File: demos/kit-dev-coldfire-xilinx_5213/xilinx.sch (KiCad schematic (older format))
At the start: 21 parts, among them P1 CONN_6, P3 CONN_2X2, P4 CONN_20X2, U9 XCR3256-TQ144

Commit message: Update demos to use sym-lib-table and recent libraries
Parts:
- C51, C52, C53, C54, C55, C56, C57, C58, C59, C60, C61: symbol C -> kit-dev-coldfire-xilinx_5213_schlib:C
- D8, D9: symbol LED -> kit-dev-coldfire-xilinx_5213_schlib:LED
- P1: symbol CONN_6 -> kit-dev-coldfire-xilinx_5213_schlib:CONN_6
- P3: symbol CONN_2X2 -> kit-dev-coldfire-xilinx_5213_schlib:CONN_2X2
- P4: symbol CONN_20X2 -> kit-dev-coldfire-xilinx_5213_schlib:CONN_20X2
- R57, R62, R63, R64: symbol R -> kit-dev-coldfire-xilinx_5213_schlib:R
- U9: symbol XCR3256-TQ144 -> kit-dev-coldfire-xilinx_5213_schlib:XCR3256-TQ144
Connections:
- wire segments 172 -> 149
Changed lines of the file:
@@
-EESchema Schematic File Version 2
-LIBS:power
-LIBS:device
-LIBS:transistors
-LIBS:conn
-LIBS:linear
-LIBS:regul
-LIBS:74xx
-LIBS:adc-dac
-LIBS:memory
-LIBS:xilinx
-LIBS:special
-LIBS:microcontrollers
-LIBS:motorola
+EESchema Schematic File Version 4
 LIBS:kit-dev-coldfire-xilinx_5213-cache
-EELAYER 25 0
+EELAYER 26 0
 EELAYER END
 $Descr A4 11693 8268
@@
 	3600 3800 3400 3800
 Wire Wire Line
-	10600 6350 10600 6400
+	10600 6400 10600 6350
 Connection ~ 10000 6400
 Wire Wire Line
@@
 	8800 6400 8800 6350
 Wire Wire Line
-	10600 6400 10300 6400
-Wire Wire Line
-	10300 6400 10000 6400
-Wire Wire Line
-	10000 6400 9700 6400
-Wire Wire Line
-	9700 6400 9400 6400
-Wire Wire Line
-	9400 6400 9100 6400
-Wire Wire Line
-	9100 6400 8800 6400
-Wire Wire Line
-	8800 6400 8500 6400
-Wire Wire Line
-	8500 6400 8200 6400
-Wire Wire Line
-	8200 6400 7900 6400
-Wire Wire Line
-	7900 6400 7600 6400
-Wire Wire Line
-	7600 5900 7900 5900
-Wire Wire Line
-	7900 5900 8200 5900
-Wire Wire Line
-	8200 5900 8500 5900
-Wire Wire Line
-	8500 5900 8800 5900
-Wire Wire Line
-	8800 5900 9100 5900
-Wire Wire Line
-	9100 5900 9400 5900
-Wire Wire Line
-	9400 5900 9700 5900
-Wire Wire Line
-	9700 5900 10000 5900
-Wire Wire Line
-	10000 5900 10300 5900
-Wire Wire Line
-	10300 5900 10600 5900
+	7600 6400 10600 6400
+Wire Wire Line
+	7600 5900 10600 5900
 Connection ~ 9700 5900
 Connection ~ 9100 5900
@@
 Connection ~ 7600 5900
 Wire Wire Line
-	7600 5950 7600 5900
-Wire Wire Line
-	7600 5900 7600 5850
+	7600 5850 7600 5950
 Connection ~ 10000 5900
 Connection ~ 7900 5900
@@
 	10000 5900 10000 5950
 Wire Wire Line
-	7600 6450 7600 6400
-Wire Wire Line
-	7600 6400 7600 6350
+	7600 6350 7600 6450
 Connection ~ 7600 6400
 Wire Wire Line
@@
 	3450 1200 3450 1250
 Wire Wire Line
-	3600 900  3050 900
-Wire Wire Line
-	3050 900  2700 900
+	2700 900  3600 900
 Wire Wire Line
 	3600 3900 3550 3900
 Wire Wire Line
-	3550 3900 3550 4000
-Wire Wire Line
-	3550 4000 3550 4100
-Wire Wire Line
-	3500 4100 3550 4100
-Wire Wire Line
-	3550 4100 3600 4100
+	3550 3900 3550 4100
+Wire Wire Line
+	3500 4100 3600 4100
 Connection ~ 3550 4100
 Wire Wire Line
@@
 +3,3V_OUT
 $Comp
-L GND #PWR0105
+L kit-dev-coldfire-xilinx_5213_schlib:GND #PWR0105
 U 1 1 480DCF5A
 P 3500 4100
@@
 $EndComp
 $Comp
-L +3,3V #PWR0106
+L kit-dev-coldfire-xilinx_5213_schlib:+3,3V #PWR0106
 U 1 1 4791D619
 P 10850 3900
@@
 $EndComp
 $Comp
-L R R64
+L kit-dev-coldfire-xilinx_5213_schlib:R R64
 U 1 1 4791D59D
 P 10450 3900
@@
 NoConn ~ 5500 900
 $Comp
-L GND #PWR0107
+L kit-dev-coldfire-xilinx_5213_schlib:GND #PWR0107
 U 1 1 470F3BF2
 P 3450 1250
@@
 XIL_IRQ1
 $Comp
-L CONN_2X2 P3
+L kit-dev-coldfire-xilinx_5213_schlib:CONN_2X2 P3
 U 1 1 46A76EB2
 P 6600 1250
@@
 $EndComp
 $Comp
-L XCR3256-TQ144 U9
+L kit-dev-coldfire-xilinx_5213_schlib:XCR3256-TQ144 U9
 U 1 1 470F38BE
 P 4550 4100
@@
 XIL_D35
 $Comp
-L GND #PWR0108
+L kit-dev-coldfire-xilinx_5213_schlib:GND #PWR0108
 U 1 1 46ADE620
 P 9650 4000
@@
 $EndComp
 $Comp
-L GND #PWR0109
+L kit-dev-coldfire-xilinx_5213_schlib:GND #PWR0109
 U 1 1 46ADE61B
 P 9650 2100
@@
 XIL_D6
 $Comp
-L CONN_20X2 P4
+L kit-dev-coldfire-xilinx_5213_schlib:CONN_20X2 P4
 U 1 1 46ADE55A
 P 9200 3050
@@
 GLCK2
 $Comp
-L +3,3V #PWR0110
+L kit-dev-coldfire-xilinx_5213_schlib:+3,3V #PWR0110
 U 1 1 46A76BD3
 P 2750 1300
@@
 $EndComp
 $Comp
-L +3,3V #PWR0111
+L kit-dev-coldfire-xilinx_5213_schlib:+3,3V #PWR0111
 U 1 1 46A76BD2
 P 3600 650
@@
 $EndComp
 $Comp
-L R R57
+L kit-dev-coldfire-xilinx_5213_schlib:R R57
 U 1 1 46A76BCA
 P 3300 650
@@
 LED_TEST1
 $Comp
-L GND #PWR0112
+L kit-dev-coldfire-xilinx_5213_schlib:GND #PWR0112
 U 1 1 46A76BC5
 P 10050 5100
@@
 $EndComp
 $Comp
-L LED D8
+L kit-dev-coldfire-xilinx_5213_schlib:LED D8
 U 1 1 46A76BC4
 P 9800 5100
@@
 $EndComp
 $Comp
-L R R62
+L kit-dev-coldfire-xilinx_5213_schlib:R R62
 U 1 1 46A76BC3
 P 9250 5100
@@
 $EndComp
 $Comp
-L GND #PWR0113
+L kit-dev-coldfire-xilinx_5213_schlib:GND #PWR0113
 U 1 1 46A76BC1
 P 7600 6450
@@
 $EndComp
 $Comp
-L +3,3V #PWR0114
+L kit-dev-coldfire-xilinx_5213_schlib:+3,3V #PWR0114
 U 1 1 46A76BBF
 P 7600 5850
@@
 $EndComp
 $Comp
-L C C61
+L kit-dev-coldfire-xilinx_5213_schlib:C C61
 U 1 1 46A76BBC
 P 10600 6150
@@
 $EndComp
 $Comp
-L C C60
+L kit-dev-coldfire-xilinx_5213_schlib:C C60
 U 1 1 46A76BBB
 P 10300 6150
@@
 $EndComp
 $Comp
-L C C59
+L kit-dev-coldfire-xilinx_5213_schlib:C C59
 U 1 1 46A76BBA
 P 10000 6150
@@
 $EndComp
 $Comp
-L C C54
+L kit-dev-coldfire-xilinx_5213_schlib:C C54
 U 1 1 46A76BB5
 P 8500 6150
@@
 $EndComp
 $Comp
-L C C53
+L kit-dev-coldfire-xilinx_5213_schlib:C C53
 U 1 1 46A76BB4
 P 8200 6150
@@
 $EndComp
 $Comp
-L C C52
+L kit-dev-coldfire-xilinx_5213_schlib:C C52
 U 1 1 46A76BB3
 P 7900 6150
@@
 $EndComp
 $Comp
-L C C51
+L kit-dev-coldfire-xilinx_5213_schlib:C C51
 U 1 1 46A76BB2
 P 7600 6150
@@
 $EndComp
 $Comp
-L C C58
+L kit-dev-coldfire-xilinx_5213_schlib:C C58
 U 1 1 46A76BB1
 P 9700 6150
@@
 $EndComp
 $Comp
-L C C57
+L kit-dev-coldfire-xilinx_5213_schlib:C C57
 U 1 1 46A76BB0
 P 9400 6150
@@
 $EndComp
 $Comp
-L C C56
+L kit-dev-coldfire-xilinx_5213_schlib:C C56
 U 1 1 46A76BAF
 P 9100 6150
@@
 $EndComp
 $Comp
-L C C55
+L kit-dev-coldfire-xilinx_5213_schlib:C C55
 U 1 1 46A76BAE
 P 8800 6150
@@
 TCK
 $Comp
-L GND #PWR0115
+L kit-dev-coldfire-xilinx_5213_schlib:GND #PWR0115
 U 1 1 46A76BA9
 P 10050 5400
@@
 $EndComp
 $Comp
-L LED D9
+L kit-dev-coldfire-xilinx_5213_schlib:LED D9
 U 1 1 46A76BA8
 P 9800 5400
@@
 $EndComp
 $Comp
-L R R63
+L kit-dev-coldfire-xilinx_5213_schlib:R R63
 U 1 1 46A76BA7
 P 9250 5400
@@
 TDO
 $Comp
-L CONN_6 P1
+L kit-dev-coldfire-xilinx_5213_schlib:CONN_6 P1
 U 1 1 46A76BA6
 P 2350 1050
@@
 $EndComp
 $Comp
-L GND #PWR0116
+L kit-dev-coldfire-xilinx_5213_schlib:GND #PWR0116
 U 1 1 46A76BA5
 P 2750 1200

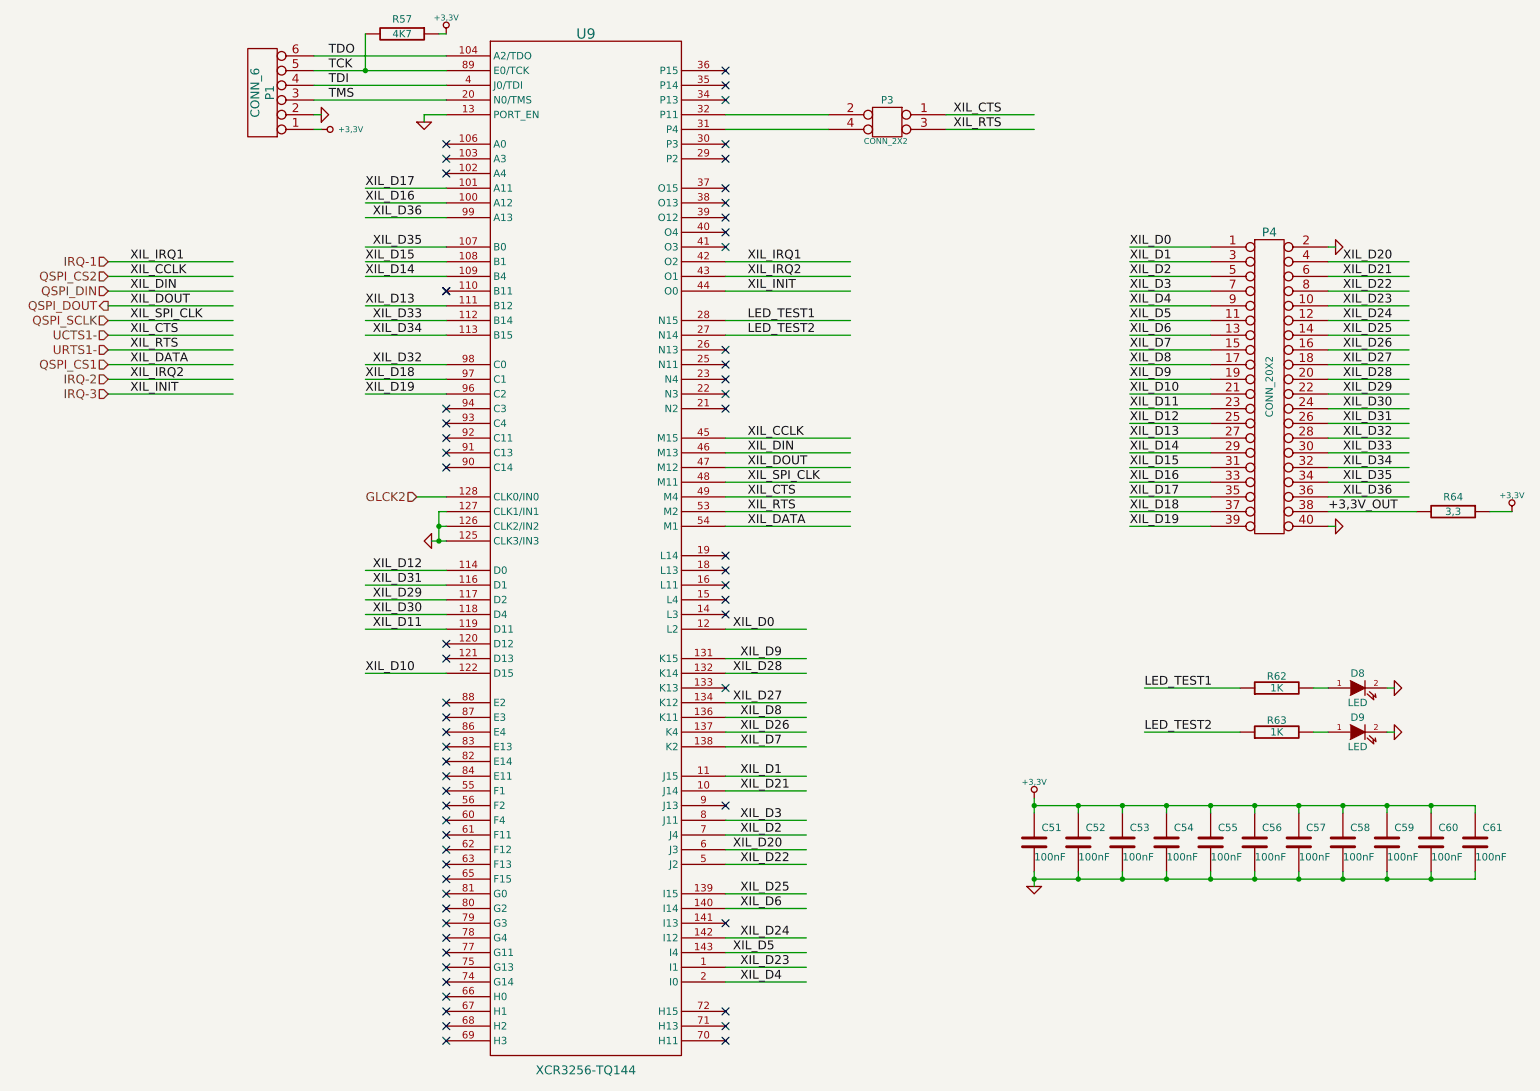
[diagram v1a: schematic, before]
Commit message: Update demo to use V5 libraries.
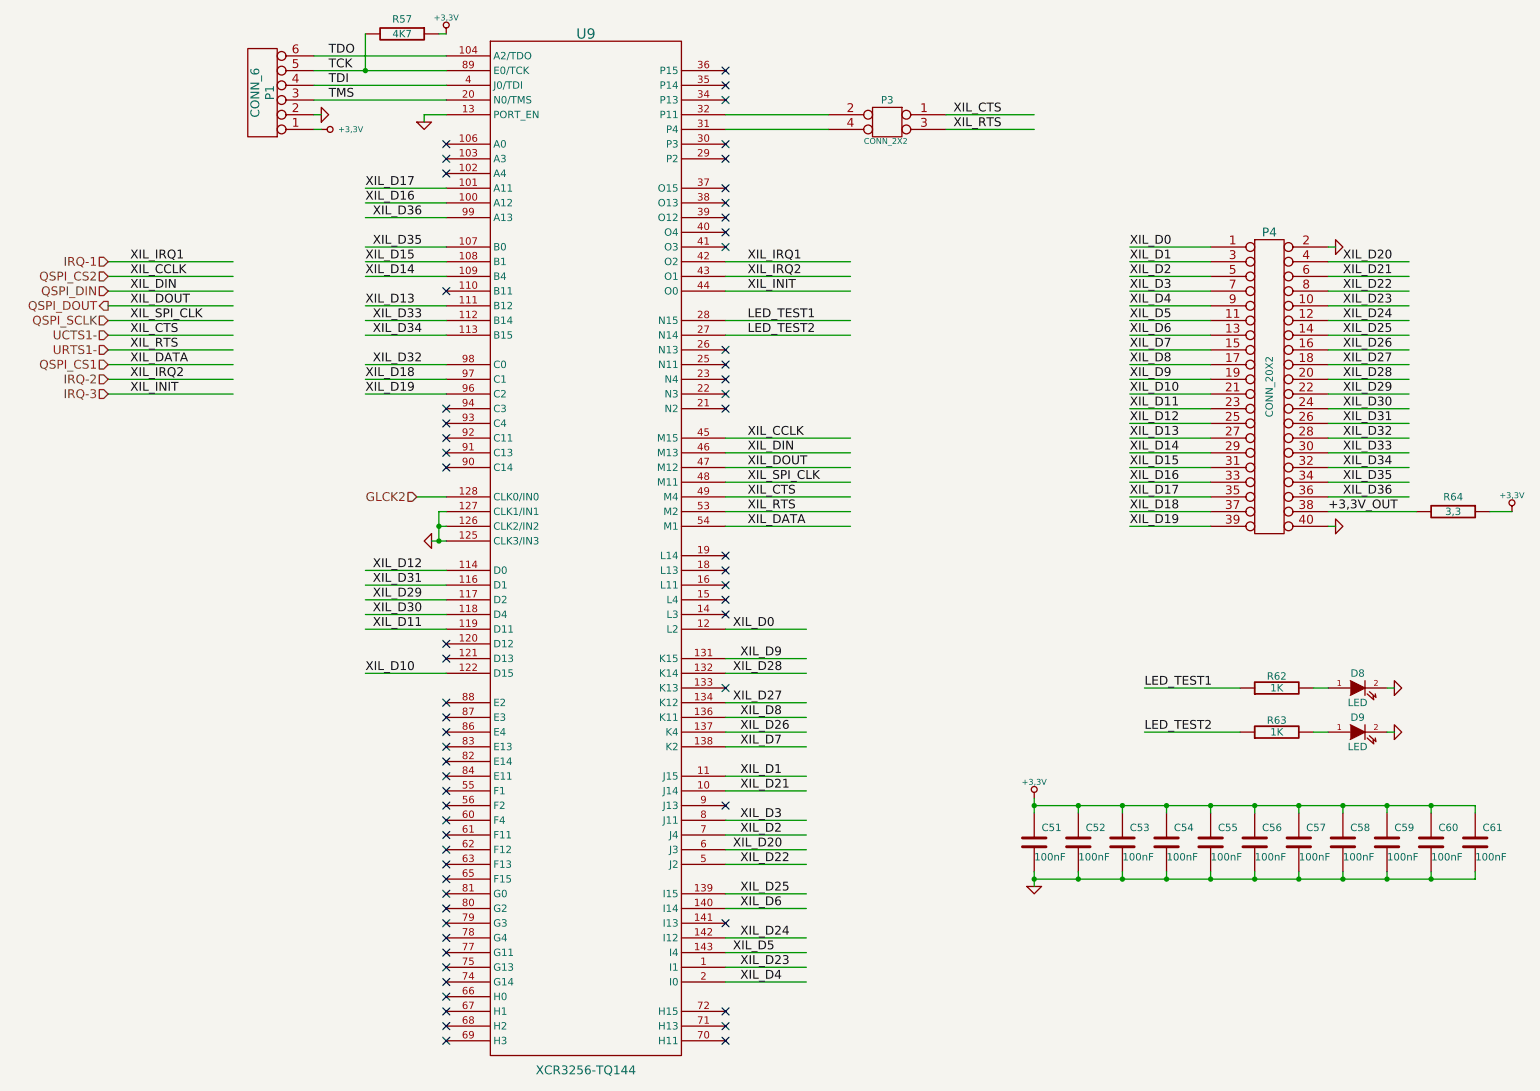
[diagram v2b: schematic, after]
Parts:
- C51, C52, C53, C54, C55, C56, C57, C58, C59, C60, C61, R57, R62, R63: footprint lib_smd:SM0805 -> Resistor_SMD:R_0805_2012Metric
- D8, D9: footprint lib_smd:SM1206POL -> LED_SMD:LED_1206_3216Metric
- P1: footprint pin_array:PIN_ARRAY-6X1 -> Connector_PinHeader_2.54mm:PinHeader_1x06_P2.54mm_Vertical
- P3: footprint pin_array:PIN_ARRAY_2X2 -> Connector_PinHeader_2.54mm:PinHeader_2x02_P2.54mm_Vertical
- P4: footprint pin_array:PIN_ARRAY_20X2 -> Connector_PinHeader_2.54mm:PinHeader_2x20_P2.54mm_Vertical
- R64: footprint discret:R4 -> Resistor_THT:R_Axial_DIN0207_L6.3mm_D2.5mm_P10.16mm_Horizontal
- U9: footprint lib_smd:TQFP144 -> Package_QFP:TQFP-144_20x20mm_P0.5mm
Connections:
- wire segments 149 -> 172
- no-connect marks 62 -> 61
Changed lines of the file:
@@
 NoConn ~ 3600 3300
 NoConn ~ 3600 3200
-NoConn ~ 3600 2400
 NoConn ~ 3600 4900
 NoConn ~ 3600 4800
@@
 	8800 6400 8800 6350
 Wire Wire Line
-	7600 6400 10600 6400
-Wire Wire Line
-	7600 5900 10600 5900
+	7600 6400 7900 6400
+Wire Wire Line
+	7600 5900 7900 5900
 Connection ~ 9700 5900
 Connection ~ 9100 5900
@@
 Connection ~ 7600 5900
 Wire Wire Line
-	7600 5850 7600 5950
+	7600 5850 7600 5900
 Connection ~ 10000 5900
 Connection ~ 7900 5900
@@
 	10000 5900 10000 5950
 Wire Wire Line
-	7600 6350 7600 6450
+	7600 6350 7600 6400
 Connection ~ 7600 6400
 Wire Wire Line
@@
 	3450 1200 3450 1250
 Wire Wire Line
-	2700 900  3600 900
+	2700 900  3050 900
 Wire Wire Line
 	3600 3900 3550 3900
 Wire Wire Line
-	3550 3900 3550 4100
-Wire Wire Line
-	3500 4100 3600 4100
+	3550 3900 3550 4000
+Wire Wire Line
+	3500 4100 3550 4100
 Connection ~ 3550 4100
 Wire Wire Line
@@
 F 0 "R64" V 10350 3900 50  0000 C CNN
 F 1 "3,3" V 10450 3900 50  0000 C CNN
-F 2 "discret:R4" H 10450 3900 60  0001 C CNN
+F 2 "Resistor_THT:R_Axial_DIN0207_L6.3mm_D2.5mm_P10.16mm_Horizontal" H 10450 3900 60  0001 C CNN
 F 3 "" H 10450 3900 60  0001 C CNN
 	1    10450 3900
@@
 F 0 "P3" H 6600 1400 50  0000 C CNN
 F 1 "CONN_2X2" H 6610 1120 40  0000 C CNN
-F 2 "pin_array:PIN_ARRAY_2X2" H 6600 1250 60  0001 C CNN
+F 2 "Connector_PinHeader_2.54mm:PinHeader_2x02_P2.54mm_Vertical" H 6600 1250 60  0001 C CNN
 F 3 "" H 6600 1250 60  0001 C CNN
 	1    6600 1250
@@
 F 0 "U9" H 4550 7550 70  0000 C CNN
 F 1 "XCR3256-TQ144" H 4550 500 60  0000 C CNN
-F 2 "lib_smd:TQFP144" H 4550 4100 60  0001 C CNN
+F 2 "Package_QFP:TQFP-144_20x20mm_P0.5mm" H 4550 4100 60  0001 C CNN
 F 3 "" H 4550 4100 60  0001 C CNN
 	1    4550 4100
@@
 F 0 "P4" H 9200 4100 60  0000 C CNN
 F 1 "CONN_20X2" V 9200 3050 50  0000 C CNN
-F 2 "pin_array:PIN_ARRAY_20X2" H 9200 3050 60  0001 C CNN
+F 2 "Connector_PinHeader_2.54mm:PinHeader_2x20_P2.54mm_Vertical" H 9200 3050 60  0001 C CNN
 F 3 "" H 9200 3050 60  0001 C CNN
 	1    9200 3050
@@
 F 0 "R57" V 3200 650 50  0000 C CNN
 F 1 "4K7" V 3300 650 50  0000 C CNN
-F 2 "lib_smd:SM0805" H 3300 650 60  0001 C CNN
+F 2 "Resistor_SMD:R_0805_2012Metric" H 3300 650 60  0001 C CNN
 F 3 "" H 3300 650 60  0001 C CNN
 	1    3300 650
@@
 F 0 "D8" H 9800 5200 50  0000 C CNN
 F 1 "LED" H 9800 5000 50  0000 C CNN
-F 2 "lib_smd:SM1206POL" H 9800 5100 60  0001 C CNN
+F 2 "LED_SMD:LED_1206_3216Metric" H 9800 5100 60  0001 C CNN
 F 3 "" H 9800 5100 60  0001 C CNN
 	1    9800 5100
@@
 F 0 "R62" V 9330 5100 50  0000 C CNN
 F 1 "1K" V 9250 5100 50  0000 C CNN
-F 2 "lib_smd:SM0805" H 9250 5100 60  0001 C CNN
+F 2 "Resistor_SMD:R_0805_2012Metric" H 9250 5100 60  0001 C CNN
 F 3 "" H 9250 5100 60  0001 C CNN
 	1    9250 5100
@@
 F 0 "C61" H 10650 6250 50  0000 L CNN
 F 1 "100nF" H 10600 6050 50  0000 L CNN
-F 2 "lib_smd:SM0805" H 10600 6150 60  0001 C CNN
+F 2 "Resistor_SMD:R_0805_2012Metric" H 10600 6150 60  0001 C CNN
 F 3 "" H 10600 6150 60  0001 C CNN
 	1    10600 6150
@@
 F 0 "C60" H 10350 6250 50  0000 L CNN
 F 1 "100nF" H 10300 6050 50  0000 L CNN
-F 2 "lib_smd:SM0805" H 10300 6150 60  0001 C CNN
+F 2 "Resistor_SMD:R_0805_2012Metric" H 10300 6150 60  0001 C CNN
 F 3 "" H 10300 6150 60  0001 C CNN
 	1    10300 6150
@@
 F 0 "C59" H 10050 6250 50  0000 L CNN
 F 1 "100nF" H 10000 6050 50  0000 L CNN
-F 2 "lib_smd:SM0805" H 10000 6150 60  0001 C CNN
+F 2 "Resistor_SMD:R_0805_2012Metric" H 10000 6150 60  0001 C CNN
 F 3 "" H 10000 6150 60  0001 C CNN
 	1    10000 6150
@@
 F 0 "C54" H 8550 6250 50  0000 L CNN
 F 1 "100nF" H 8500 6050 50  0000 L CNN
-F 2 "lib_smd:SM0805" H 8500 6150 60  0001 C CNN
+F 2 "Resistor_SMD:R_0805_2012Metric" H 8500 6150 60  0001 C CNN
 F 3 "" H 8500 6150 60  0001 C CNN
 	1    8500 6150
@@
 F 0 "C53" H 8250 6250 50  0000 L CNN
 F 1 "100nF" H 8200 6050 50  0000 L CNN
-F 2 "lib_smd:SM0805" H 8200 6150 60  0001 C CNN
+F 2 "Resistor_SMD:R_0805_2012Metric" H 8200 6150 60  0001 C CNN
 F 3 "" H 8200 6150 60  0001 C CNN
 	1    8200 6150
@@
 F 0 "C52" H 7950 6250 50  0000 L CNN
 F 1 "100nF" H 7900 6050 50  0000 L CNN
-F 2 "lib_smd:SM0805" H 7900 6150 60  0001 C CNN
+F 2 "Resistor_SMD:R_0805_2012Metric" H 7900 6150 60  0001 C CNN
 F 3 "" H 7900 6150 60  0001 C CNN
 	1    7900 6150
@@
 F 0 "C51" H 7650 6250 50  0000 L CNN
 F 1 "100nF" H 7600 6050 50  0000 L CNN
-F 2 "lib_smd:SM0805" H 7600 6150 60  0001 C CNN
+F 2 "Resistor_SMD:R_0805_2012Metric" H 7600 6150 60  0001 C CNN
 F 3 "" H 7600 6150 60  0001 C CNN
 	1    7600 6150
@@
 F 0 "C58" H 9750 6250 50  0000 L CNN
 F 1 "100nF" H 9700 6050 50  0000 L CNN
-F 2 "lib_smd:SM0805" H 9700 6150 60  0001 C CNN
+F 2 "Resistor_SMD:R_0805_2012Metric" H 9700 6150 60  0001 C CNN
 F 3 "" H 9700 6150 60  0001 C CNN
 	1    9700 6150
@@
 F 0 "C57" H 9450 6250 50  0000 L CNN
 F 1 "100nF" H 9400 6050 50  0000 L CNN
-F 2 "lib_smd:SM0805" H 9400 6150 60  0001 C CNN
+F 2 "Resistor_SMD:R_0805_2012Metric" H 9400 6150 60  0001 C CNN
 F 3 "" H 9400 6150 60  0001 C CNN
 	1    9400 6150
@@
 F 0 "C56" H 9150 6250 50  0000 L CNN
 F 1 "100nF" H 9100 6050 50  0000 L CNN
-F 2 "lib_smd:SM0805" H 9100 6150 60  0001 C CNN
+F 2 "Resistor_SMD:R_0805_2012Metric" H 9100 6150 60  0001 C CNN
 F 3 "" H 9100 6150 60  0001 C CNN
 	1    9100 6150
@@
 F 0 "C55" H 8850 6250 50  0000 L CNN
 F 1 "100nF" H 8800 6050 50  0000 L CNN
-F 2 "lib_smd:SM0805" H 8800 6150 60  0001 C CNN
+F 2 "Resistor_SMD:R_0805_2012Metric" H 8800 6150 60  0001 C CNN
 F 3 "" H 8800 6150 60  0001 C CNN
 	1    8800 6150
@@
 F 0 "D9" H 9800 5500 50  0000 C CNN
 F 1 "LED" H 9800 5300 50  0000 C CNN
-F 2 "lib_smd:SM1206POL" H 9800 5400 60  0001 C CNN
+F 2 "LED_SMD:LED_1206_3216Metric" H 9800 5400 60  0001 C CNN
 F 3 "" H 9800 5400 60  0001 C CNN
 	1    9800 5400
@@
 F 0 "R63" V 9330 5400 50  0000 C CNN
 F 1 "1K" V 9250 5400 50  0000 C CNN
-F 2 "lib_smd:SM0805" H 9250 5400 60  0001 C CNN
+F 2 "Resistor_SMD:R_0805_2012Metric" H 9250 5400 60  0001 C CNN
 F 3 "" H 9250 5400 60  0001 C CNN
 	1    9250 5400
@@
 F 0 "P1" V 2300 1050 60  0000 C CNN
 F 1 "CONN_6" V 2400 1050 60  0000 C CNN
-F 2 "pin_array:PIN_ARRAY-6X1" H 2350 1050 60  0001 C CNN
+F 2 "Connector_PinHeader_2.54mm:PinHeader_1x06_P2.54mm_Vertical" H 2350 1050 60  0001 C CNN
 F 3 "" H 2350 1050 60  0001 C CNN
 	1    2350 1050
@@
 Wire Wire Line
 	10000 5100 10050 5100
+Wire Wire Line
+	3050 900  3600 900
+Wire Wire Line
+	3550 4000 3550 4100
+Wire Wire Line
+	10000 6400 10300 6400
+Wire Wire Line
+	9400 6400 9700 6400
+Wire Wire Line
+	8800 6400 9100 6400
+Wire Wire Line
+	9700 5900 10000 5900
+Wire Wire Line
+	9100 5900 9400 5900
+Wire Wire Line
+	8500 5900 8800 5900
+Wire Wire Line
+	7600 5900 7600 5950
+Wire Wire Line
+	10000 5900 10300 5900
+Wire Wire Line
+	7900 5900 8200 5900
+Wire Wire Line
+	8200 5900 8500 5900
+Wire Wire Line
+	8800 5900 9100 5900
+Wire Wire Line
+	9400 5900 9700 5900
+Wire Wire Line
+	8500 6400 8800 6400
+Wire Wire Line
+	10300 5900 10600 5900
+Wire Wire Line
+	7900 6400 8200 6400
+Wire Wire Line
+	8200 6400 8500 6400
+Wire Wire Line
+	7600 6400 7600 6450
+Wire Wire Line
+	9100 6400 9400 6400
+Wire Wire Line
+	9700 6400 10000 6400
+Wire Wire Line
+	10300 6400 10600 6400
+Wire Wire Line
+	3550 4100 3600 4100
 $EndSCHEMATC
